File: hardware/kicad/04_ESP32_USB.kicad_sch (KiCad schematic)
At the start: 12 parts, among them J201 GCT USB4105-GF-A, U201 ESP32-S3-MINI-1-N8

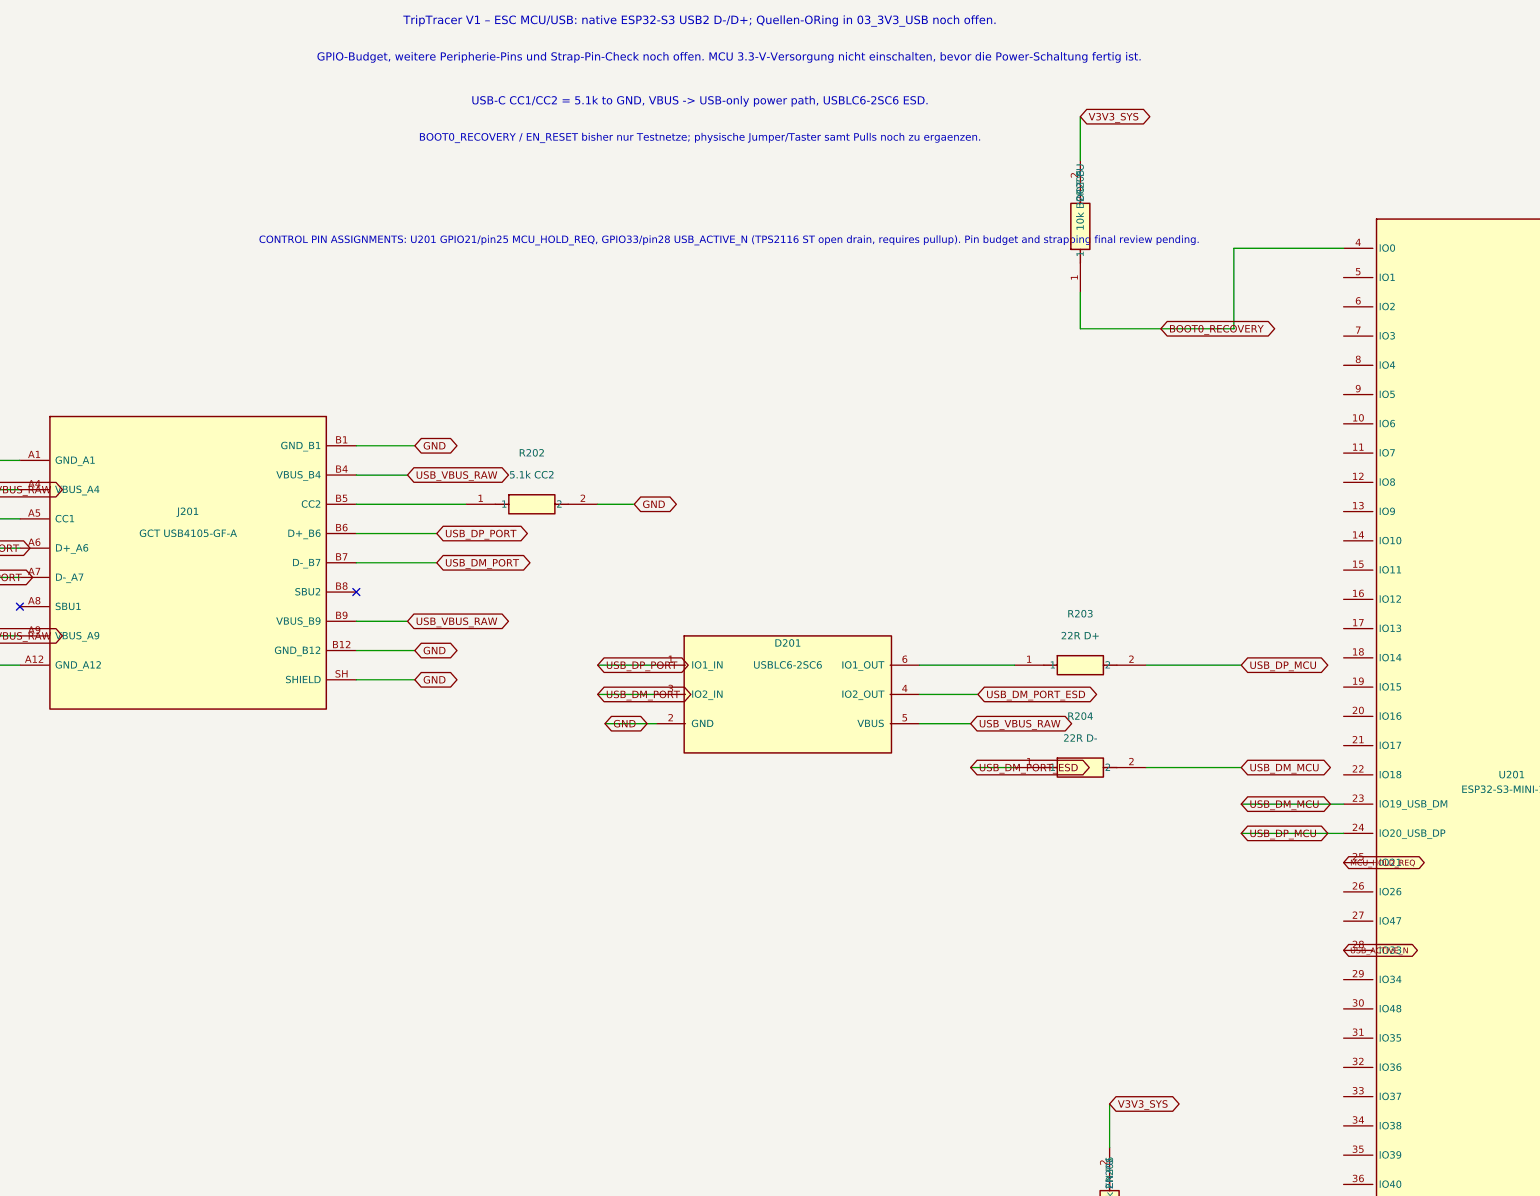
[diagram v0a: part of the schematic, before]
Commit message: Complete isolated ACC-off sensing for hardware shutdown interface
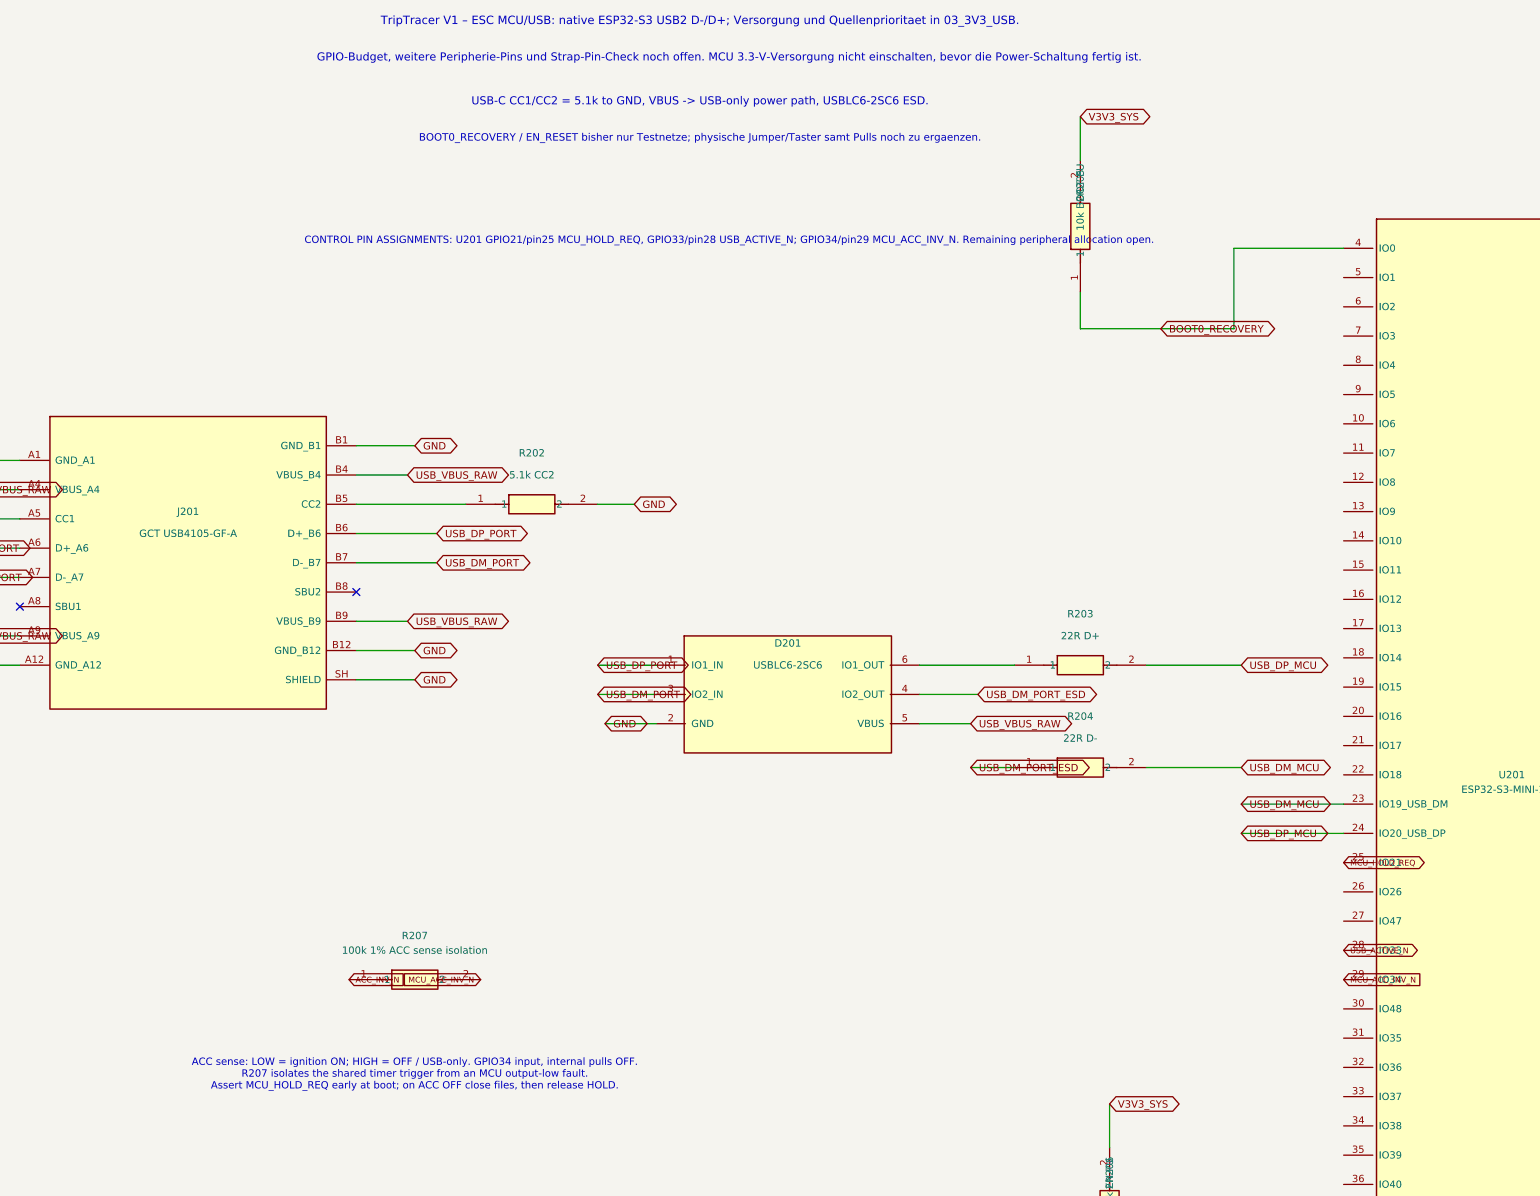
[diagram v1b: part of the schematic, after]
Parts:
- added R207: 100k 1% ACC sense isolation, Tripmaster:R_1206_3216, symbol Tripmaster_Sym:R
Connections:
- net MCU_ACC_INV_N: now reaches U201.29 (IO34)
- net MCU_ACC_INV_N: now also R207.2
- new net ACC_INV_N: R207.1
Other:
- note added: "ACC sense: LOW = ignition ON; HIGH = OFF / USB-only. GPIO34 input, internal pulls OFF. R207 isolates the shared timer trigger from an MCU output-low fault. Assert MCU_HOLD_REQ early at boot; on ACC OFF close files, then release HOLD."
- note added: "CONTROL PIN ASSIGNMENTS: U201 GPIO21/pin25 MCU_HOLD_REQ, GPIO33/pin28 USB_ACTIVE_N; GPIO34/pin29 MCU_ACC_INV_N. Remaining peripheral allocation open."
- note added: "TripTracer V1 – ESC MCU/USB: native ESP32-S3 USB2 D-/D+; Versorgung und Quellenprioritaet in 03_3V3_USB."
- note removed: "CONTROL PIN ASSIGNMENTS: U201 GPIO21/pin25 MCU_HOLD_REQ, GPIO33/pin28 USB_ACTIVE_N (TPS2116 ST open drain, requires pullup). Pin budget and strapping final review pending."
- note removed: "TripTracer V1 – ESC MCU/USB: native ESP32-S3 USB2 D-/D+; Quellen-ORing in 03_3V3_USB noch offen."
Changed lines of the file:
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@@
 (kicad_sch (version 20250114) (generator "eeschema")
 (paper "A2") (title_block (title "TripTracer V1 – ESP32-S3 / native USB-C – Arbeitsstand") (date "2026-10-13") (rev "a1 / NICHT ERC-GEPRUEFT"))
-(text "TripTracer V1 – ESC MCU/USB: native ESP32-S3 USB2 D-/D+; Quellen-ORing in 03_3V3_USB noch offen." (at 199.39 16.51 0) (effects (font (size 1.45 1.45))))
+(text "TripTracer V1 – ESC MCU/USB: native ESP32-S3 USB2 D-/D+; Versorgung und Quellenprioritaet in 03_3V3_USB." (at 199.39 16.51 0) (effects (font (size 1.45 1.45))))
 (text "GPIO-Budget, weitere Peripherie-Pins und Strap-Pin-Check noch offen. MCU 3.3-V-Versorgung nicht einschalten, bevor die Power-Schaltung fertig ist." (at 204.47 22.86 0) (effects (font (size 1.4 1.4))))
 (text "USB-C CC1/CC2 = 5.1k to GND, VBUS -> USB-only power path, USBLC6-2SC6 ESD." (at 199.39 30.48 0) (effects (font (size 1.4 1.4))))
@@
 (global_label "MCU_HOLD_REQ" (shape bidirectional) (at 311.15 162.56 0) (effects (font (size 1.0 1.0)) (justify left)))
 (global_label "USB_ACTIVE_N" (shape bidirectional) (at 311.15 177.8 0) (effects (font (size 1.0 1.0)) (justify left)))
-(text "CONTROL PIN ASSIGNMENTS: U201 GPIO21/pin25 MCU_HOLD_REQ, GPIO33/pin28 USB_ACTIVE_N (TPS2116 ST open drain, requires pullup). Pin budget and strapping final review pending." (at 204.47 54.61 0) (effects (font (size 1.27 1.27))))
+(text "CONTROL PIN ASSIGNMENTS: U201 GPIO21/pin25 MCU_HOLD_REQ, GPIO33/pin28 USB_ACTIVE_N; GPIO34/pin29 MCU_ACC_INV_N. Remaining peripheral allocation open." (at 204.47 54.61 0) (effects (font (size 1.27 1.27))))
 (sheet_instances (path "/" (page "5"))) (embedded_fonts no)
+(symbol (lib_id "Tripmaster_Sym:R") (at 149.86 182.88 0) (unit 1) (exclude_from_sim no) (in_bom yes) (on_board yes) (dnp no)
+ (property "Reference" "R207" (at 149.86 175.26 0) (effects (font (size 1.27 1.27))))
+ (property "Value" "100k 1% ACC sense isolation" (at 149.86 177.8 0) (effects (font (size 1.27 1.27))))
+ (property "Footprint" "Tripmaster:R_1206_3216" (at 149.86 182.88 0) (effects (font (size 1.27 1.27)) (hide yes)))
+ (pin "1") (pin "2")
+ (instances (project "TripTracer_V1" (path "/a26d9b0c-7f10-4e5a-a65f-000000000064/a26d9b0c-7f10-4e5a-a65f-000000000068" (reference "R207") (unit 1)))))
+(global_label "ACC_INV_N" (shape input) (at 138.43 182.88 0) (effects (font (size 1.0 1.0)) (justify left)))
+(global_label "MCU_ACC_INV_N" (shape input) (at 161.29 182.88 180) (effects (font (size 1.0 1.0)) (justify right)))
+(global_label "MCU_ACC_INV_N" (shape input) (at 311.15 182.88 0) (effects (font (size 1.0 1.0)) (justify left)))
+(text "ACC sense: LOW = ignition ON; HIGH = OFF / USB-only. GPIO34 input, internal pulls OFF.\nR207 isolates the shared timer trigger from an MCU output-low fault.\nAssert MCU_HOLD_REQ early at boot; on ACC OFF close files, then release HOLD." (at 149.86 199.39 0) (effects (font (size 1.27 1.27))))
 )

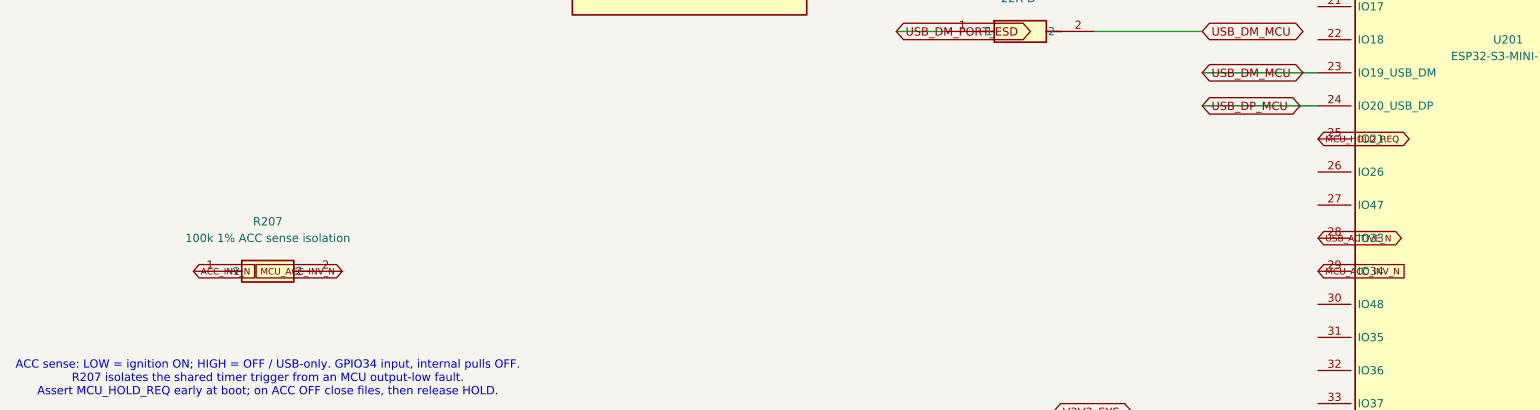
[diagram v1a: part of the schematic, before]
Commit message: Make input protection and ACC interfaces readable in native schematic PDF
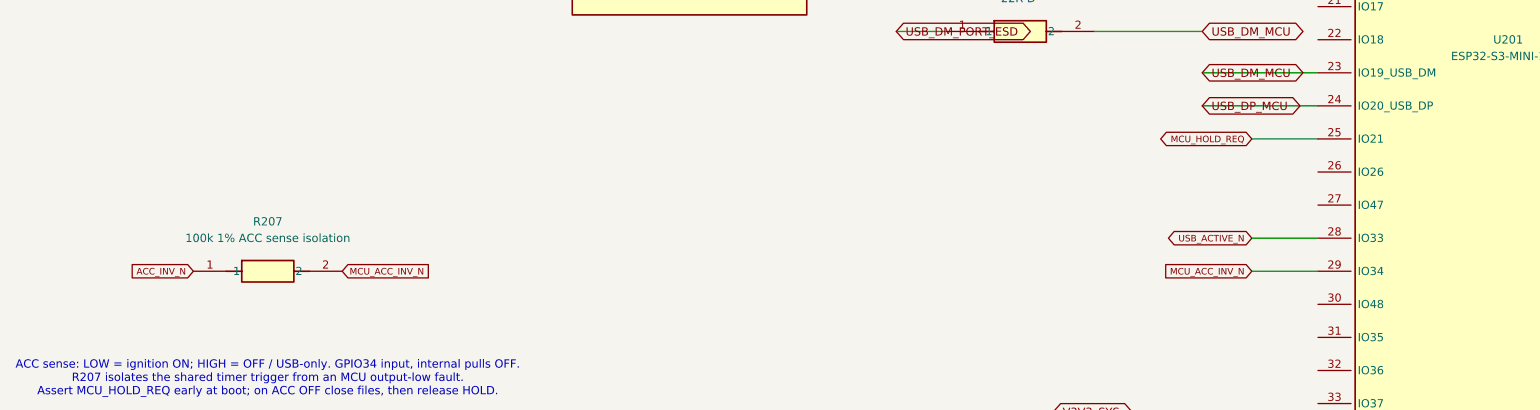
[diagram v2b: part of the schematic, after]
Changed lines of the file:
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@@
 (junction (at 387.35 210.82) (diameter 0) (color 0 0 0 0))
 (junction (at 387.35 215.9) (diameter 0) (color 0 0 0 0))
-(global_label "MCU_HOLD_REQ" (shape bidirectional) (at 311.15 162.56 0) (effects (font (size 1.0 1.0)) (justify left)))
-(global_label "USB_ACTIVE_N" (shape bidirectional) (at 311.15 177.8 0) (effects (font (size 1.0 1.0)) (justify left)))
+(global_label "MCU_HOLD_REQ" (shape bidirectional) (at 300.99 162.56 180) (effects (font (size 1.0 1.0)) (justify right)))
+(global_label "USB_ACTIVE_N" (shape bidirectional) (at 300.99 177.8 180) (effects (font (size 1.0 1.0)) (justify right)))
 (text "CONTROL PIN ASSIGNMENTS: U201 GPIO21/pin25 MCU_HOLD_REQ, GPIO33/pin28 USB_ACTIVE_N; GPIO34/pin29 MCU_ACC_INV_N. Remaining peripheral allocation open." (at 204.47 54.61 0) (effects (font (size 1.27 1.27))))
 (sheet_instances (path "/" (page "5"))) (embedded_fonts no)
@@
  (pin "1") (pin "2")
  (instances (project "TripTracer_V1" (path "/a26d9b0c-7f10-4e5a-a65f-000000000064/a26d9b0c-7f10-4e5a-a65f-000000000068" (reference "R207") (unit 1)))))
-(global_label "ACC_INV_N" (shape input) (at 138.43 182.88 0) (effects (font (size 1.0 1.0)) (justify left)))
-(global_label "MCU_ACC_INV_N" (shape input) (at 161.29 182.88 180) (effects (font (size 1.0 1.0)) (justify right)))
-(global_label "MCU_ACC_INV_N" (shape input) (at 311.15 182.88 0) (effects (font (size 1.0 1.0)) (justify left)))
+(global_label "ACC_INV_N" (shape input) (at 138.43 182.88 180) (effects (font (size 1.0 1.0)) (justify right)))
+(global_label "MCU_ACC_INV_N" (shape input) (at 161.29 182.88 0) (effects (font (size 1.0 1.0)) (justify left)))
+(global_label "MCU_ACC_INV_N" (shape input) (at 300.99 182.88 180) (effects (font (size 1.0 1.0)) (justify right)))
 (text "ACC sense: LOW = ignition ON; HIGH = OFF / USB-only. GPIO34 input, internal pulls OFF.\nR207 isolates the shared timer trigger from an MCU output-low fault.\nAssert MCU_HOLD_REQ early at boot; on ACC OFF close files, then release HOLD." (at 149.86 199.39 0) (effects (font (size 1.27 1.27))))
+(wire (pts (xy 300.99 162.56) (xy 311.15 162.56)) (stroke (width 0) (type default)))
+(wire (pts (xy 300.99 177.8) (xy 311.15 177.8)) (stroke (width 0) (type default)))
+(wire (pts (xy 300.99 182.88) (xy 311.15 182.88)) (stroke (width 0) (type default)))
 )
